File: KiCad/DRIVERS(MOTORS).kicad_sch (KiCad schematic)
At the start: 17 parts, among them M1 Motor_DC, M2 Motor_DC, M4 Motor_DC, U1 TB6612FNG, U2 DRV8871DDA, U3 ATtiny1616-M

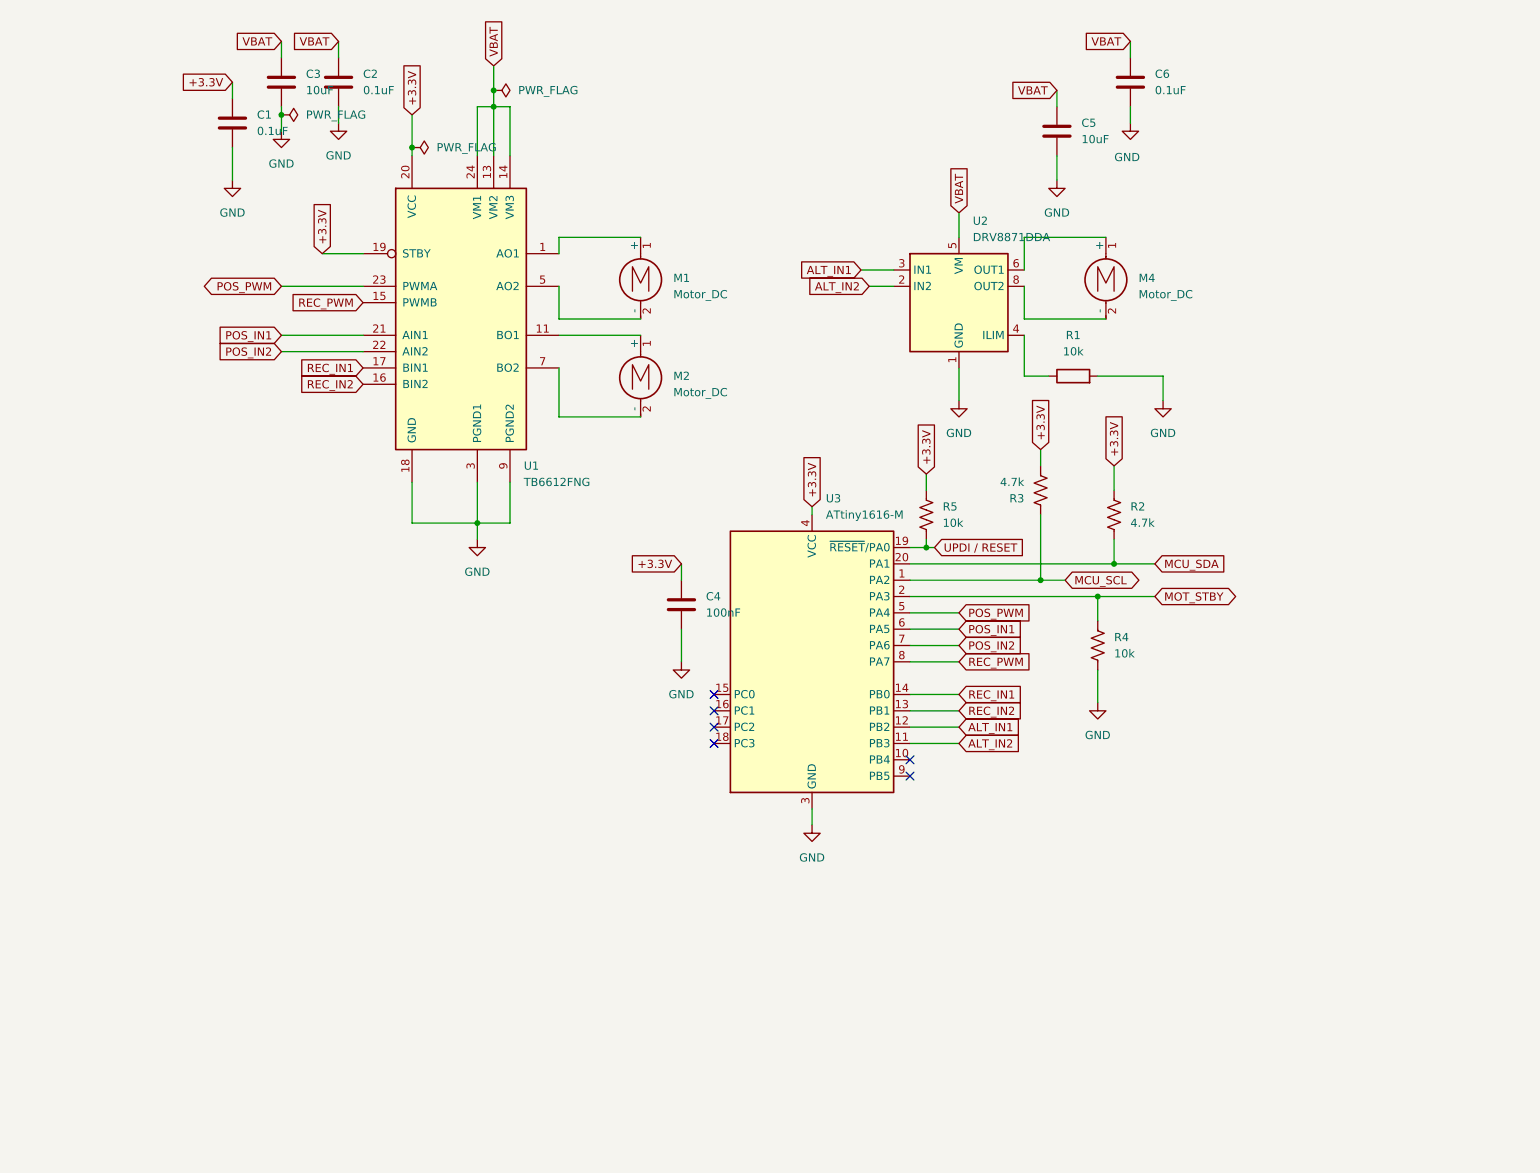
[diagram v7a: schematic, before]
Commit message: Començat el LAYOUT
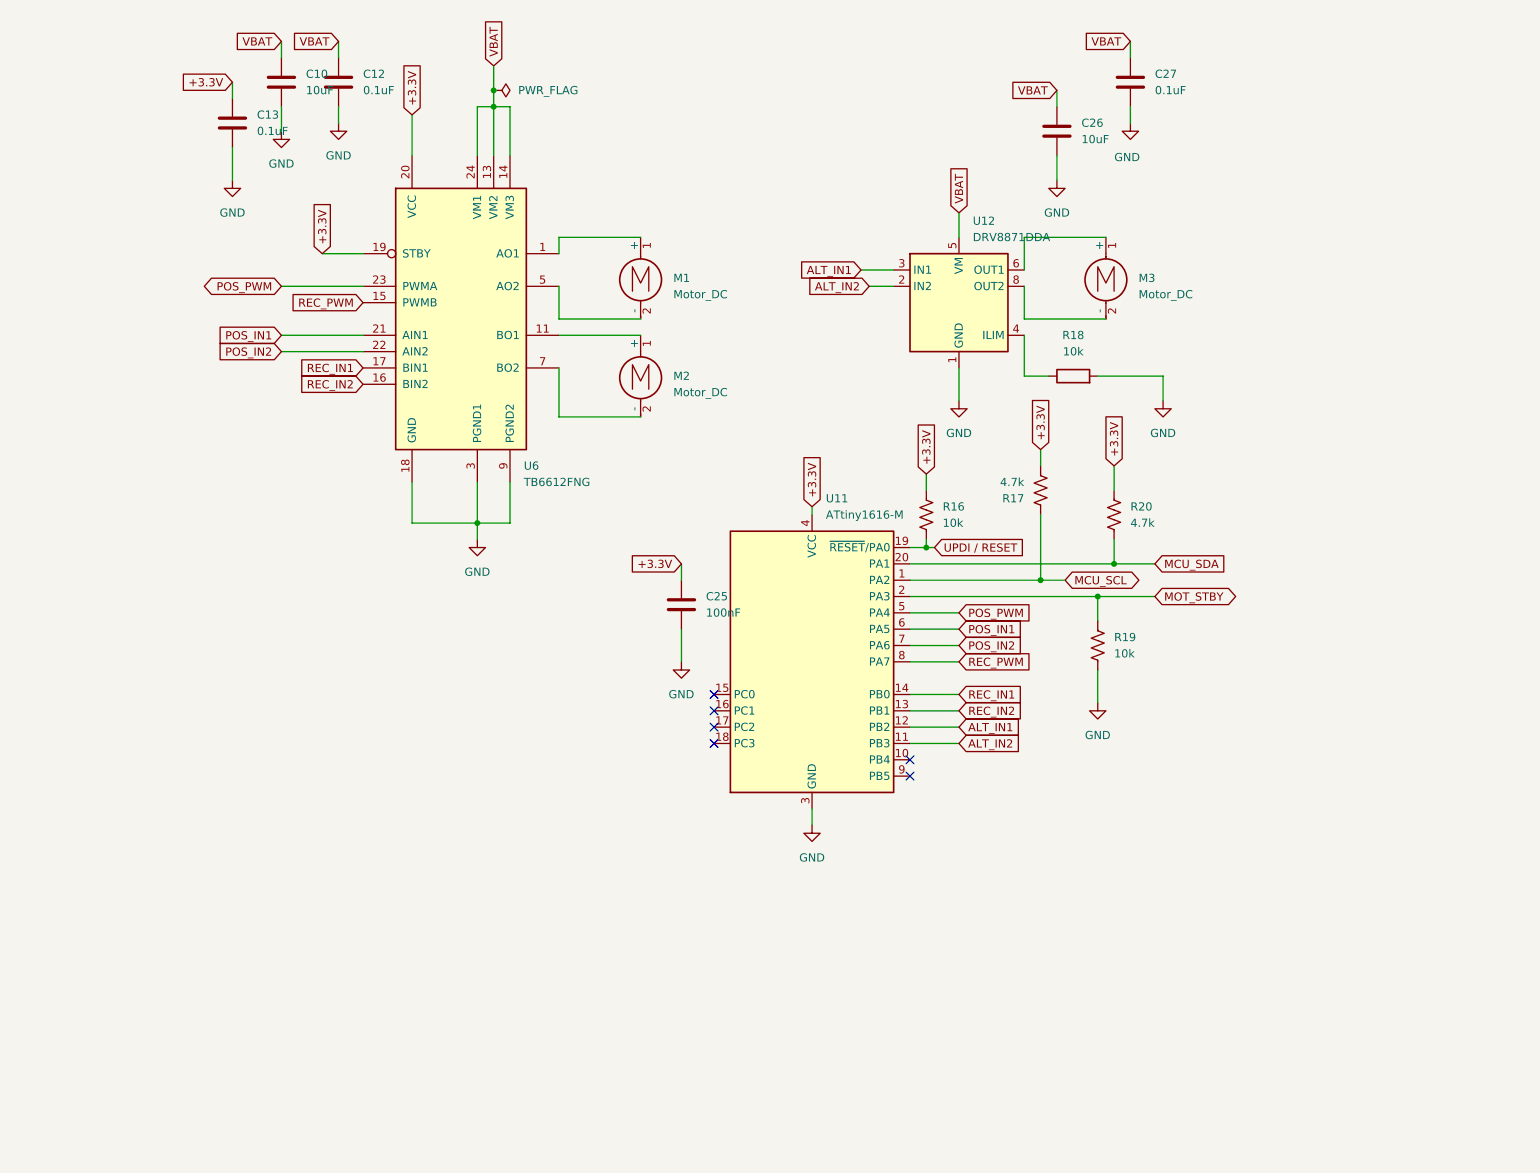
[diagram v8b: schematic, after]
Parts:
- renumbered C3 to C10, C2 to C12, C1 to C13, C4 to C25, C5 to C26, C6 to C27, M4 to M3, R5 to R16, R3 to R17, R1 to R18, R4 to R19, R2 to R20, U3 to U11, U2 to U12, U1 to U6
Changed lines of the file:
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@@
 	)
 	(junction
-		(at 87.63 29.21)
-		(diameter 0)
-		(color 0 0 0 0)
-	)
-	(junction
 		(at 205.74 101.6)
 		(diameter 0)
@@
 	)
 	(junction
-		(at 107.95 34.29)
-		(diameter 0)
-		(color 0 0 0 0)
-	)
-	(junction
 		(at 118.11 92.71)
 		(diameter 0)
@@
 	(wire
 		(pts
-			(xy 107.95 29.21) (xy 107.95 34.29)
+			(xy 107.95 29.21) (xy 107.95 35.56)
 		)
 		(stroke
@@
 	(wire
 		(pts
-			(xy 107.95 34.29) (xy 107.95 35.56)
-		)
-		(stroke
-			(width 0)
-			(type default)
-		)
-	)
-	(wire
-		(pts
 			(xy 123.19 92.71) (xy 118.11 92.71)
 		)
@@
 	(wire
 		(pts
-			(xy 87.63 29.21) (xy 87.63 31.75)
-		)
-		(stroke
-			(width 0)
-			(type default)
-		)
-	)
-	(wire
-		(pts
 			(xy 205.74 101.6) (xy 209.55 101.6)
 		)
@@
 	(wire
 		(pts
-			(xy 87.63 27.94) (xy 87.63 29.21)
+			(xy 87.63 27.94) (xy 87.63 31.75)
 		)
 		(stroke
@@
 		(dnp no)
 		(fields_autoplaced yes)
-		(property "Reference" "R1"
+		(property "Reference" "R18"
 			(at 210.82 63.5 90)
 			(effects
@@
 		(dnp no)
 		(fields_autoplaced yes)
-		(property "Reference" "U2"
+		(property "Reference" "U12"
 			(at 195.1833 45.72 0)
 			(effects
@@
 		(dnp no)
 		(fields_autoplaced yes)
-		(property "Reference" "R3"
+		(property "Reference" "R17"
 			(at 203.2 88.9001 0)
 			(effects
@@
 		(dnp no)
 		(fields_autoplaced yes)
-		(property "Reference" "C5"
+		(property "Reference" "C26"
 			(at 212.09 30.4799 0)
 			(effects
@@
 		(dnp no)
 		(fields_autoplaced yes)
-		(property "Reference" "C3"
+		(property "Reference" "C10"
 			(at 91.44 22.8599 0)
 			(effects
@@
 		(dnp no)
 		(fields_autoplaced yes)
-		(property "Reference" "C6"
+		(property "Reference" "C27"
 			(at 223.52 22.8599 0)
 			(effects
@@
 		(dnp no)
 		(fields_autoplaced yes)
-		(property "Reference" "#PWR02"
+		(property "Reference" "#PWR018"
 			(at 96.52 36.83 0)
 			(effects
@@
 		(dnp no)
 		(fields_autoplaced yes)
-		(property "Reference" "#PWR04"
+		(property "Reference" "#PWR021"
 			(at 118.11 101.6 0)
 			(effects
@@
 		(dnp no)
 		(fields_autoplaced yes)
-		(property "Reference" "C4"
+		(property "Reference" "C25"
 			(at 153.67 104.1399 0)
 			(effects
@@
 	)
 	(symbol
-		(lib_id "power:PWR_FLAG")
-		(at 107.95 34.29 270)
-		(unit 1)
-		(exclude_from_sim no)
-		(in_bom yes)
-		(on_board yes)
-		(dnp no)
-		(fields_autoplaced yes)
-		(property "Reference" "#FLG02"
-			(at 109.855 34.29 0)
-			(effects
-				(font
-					(size 1.27 1.27)
-				)
-				(hide yes)
-			)
-		)
-		(property "Value" "PWR_FLAG"
-			(at 111.76 34.2899 90)
-			(effects
-				(font
-					(size 1.27 1.27)
-				)
-				(justify left)
-			)
-		)
-		(property "Footprint" ""
-			(at 107.95 34.29 0)
-			(effects
-				(font
-					(size 1.27 1.27)
-				)
-				(hide yes)
-			)
-		)
-		(property "Datasheet" "~"
-			(at 107.95 34.29 0)
-			(effects
-				(font
-					(size 1.27 1.27)
-				)
-				(hide yes)
-			)
-		)
-		(property "Description" "Special symbol for telling ERC where power comes from"
-			(at 107.95 34.29 0)
-			(effects
-				(font
-					(size 1.27 1.27)
-				)
-				(hide yes)
-			)
-		)
-		(pin "1"
-		)
-		(instances
-			(project "DRIVERS(MOTORS)"
-				(path "/7b02ed73-5e8a-4db8-ad9f-4f6390d1b355"
-					(reference "#FLG02")
-					(unit 1)
-				)
-			)
-		)
-	)
-	(symbol
 		(lib_id "power:GND")
 		(at 80.01 39.37 0)
@@
 		(dnp no)
 		(fields_autoplaced yes)
-		(property "Reference" "#PWR03"
+		(property "Reference" "#PWR019"
 			(at 80.01 45.72 0)
 			(effects
@@
 		(dnp no)
 		(fields_autoplaced yes)
-		(property "Reference" "#FLG03"
+		(property "Reference" "#FLG011"
 			(at 122.555 25.4 0)
 			(effects
@@
 		(dnp no)
 		(fields_autoplaced yes)
-		(property "Reference" "#PWR05"
+		(property "Reference" "#PWR041"
 			(at 193.04 80.01 0)
 			(effects
@@
 		(on_board yes)
 		(dnp no)
-		(property "Reference" "#PWR011"
+		(property "Reference" "#PWR044"
 			(at 219.71 36.83 0)
 			(effects
@@
 		(dnp no)
 		(fields_autoplaced yes)
-		(property "Reference" "#PWR07"
+		(property "Reference" "#PWR040"
 			(at 170.18 146.05 0)
 			(effects
@@
 		(dnp no)
 		(fields_autoplaced yes)
-		(property "Reference" "M4"
+		(property "Reference" "M3"
 			(at 220.98 54.6099 0)
 			(effects
@@
 		(dnp no)
 		(fields_autoplaced yes)
-		(property "Reference" "R2"
+		(property "Reference" "R20"
 			(at 219.71 90.1699 0)
 			(effects
@@
 		(dnp no)
 		(fields_autoplaced yes)
-		(property "Reference" "U1"
+		(property "Reference" "U6"
 			(at 125.3333 83.82 0)
 			(effects
@@
 		(dnp no)
 		(fields_autoplaced yes)
-		(property "Reference" "U3"
+		(property "Reference" "U11"
 			(at 172.3233 88.9 0)
 			(effects
@@
 		(dnp no)
 		(fields_autoplaced yes)
-		(property "Reference" "#PWR06"
+		(property "Reference" "#PWR045"
 			(at 224.79 80.01 0)
 			(effects
@@
 		(dnp no)
 		(fields_autoplaced yes)
-		(property "Reference" "#PWR01"
+		(property "Reference" "#PWR016"
 			(at 87.63 38.1 0)
 			(effects
@@
 	)
 	(symbol
-		(lib_id "power:PWR_FLAG")
-		(at 87.63 29.21 270)
-		(unit 1)
-		(exclude_from_sim no)
-		(in_bom yes)
-		(on_board yes)
-		(dnp no)
-		(fields_autoplaced yes)
-		(property "Reference" "#FLG01"
-			(at 89.535 29.21 0)
-			(effects
-				(font
-					(size 1.27 1.27)
-				)
-				(hide yes)
-			)
-		)
-		(property "Value" "PWR_FLAG"
-			(at 91.44 29.2099 90)
-			(effects
-				(font
-					(size 1.27 1.27)
-				)
-				(justify left)
-			)
-		)
-		(property "Footprint" ""
-			(at 87.63 29.21 0)
-			(effects
-				(font
-					(size 1.27 1.27)
-				)
-				(hide yes)
-			)
-		)
-		(property "Datasheet" "~"
-			(at 87.63 29.21 0)
-			(effects
-				(font
-					(size 1.27 1.27)
-				)
-				(hide yes)
-			)
-		)
-		(property "Description" "Special symbol for telling ERC where power comes from"
-			(at 87.63 29.21 0)
-			(effects
-				(font
-					(size 1.27 1.27)
-				)
-				(hide yes)
-			)
-		)
-		(pin "1"
-		)
-		(instances
-			(project "DRIVERS(MOTORS)"
-				(path "/7b02ed73-5e8a-4db8-ad9f-4f6390d1b355"
-					(reference "#FLG01")
-					(unit 1)
-				)
-			)
-		)
-	)
-	(symbol
 		(lib_id "power:GND")
 		(at 208.28 39.37 0)
@@
 		(dnp no)
 		(fields_autoplaced yes)
-		(property "Reference" "#PWR010"
+		(property "Reference" "#PWR042"
 			(at 208.28 45.72 0)
 			(effects
@@
 		(dnp no)
 		(fields_autoplaced yes)
-		(property "Reference" "R5"
+		(property "Reference" "R16"
 			(at 190.5 90.1699 0)
 			(effects
@@
 		(dnp no)
 		(fields_autoplaced yes)
-		(property "Reference" "C2"
+		(property "Reference" "C12"
 			(at 100.33 22.8599 0)
 			(effects
@@
 		(dnp no)
 		(fields_autoplaced yes)
-		(property "Reference" "#PWR08"
+		(property "Reference" "#PWR039"
 			(at 149.86 120.65 0)
 			(effects
@@
 		(dnp no)
 		(fields_autoplaced yes)
-		(property "Reference" "#PWR09"
+		(property "Reference" "#PWR043"
 			(at 214.63 127 0)
 			(effects
@@
 		(dnp no)
 		(fields_autoplaced yes)
-		(property "Reference" "C1"
+		(property "Reference" "C13"
 			(at 83.82 29.2099 0)
 			(effects
@@
 		(dnp no)
 		(fields_autoplaced yes)
-		(property "Reference" "R4"
+		(property "Reference" "R19"
 			(at 217.17 110.4899 0)
 			(effects
